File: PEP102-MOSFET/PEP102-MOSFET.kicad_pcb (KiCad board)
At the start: 2 copper layers, 45 x 45 mm, 22 parts, among them J1 Screw_Terminal_01x02, J2 Screw_Terminal_01x02, J3 Screw_Terminal_01x02, J4 Screw_Terminal_01x02, J5 Screw_Terminal_01x02, Q13 AO3400A, Q8 AO3401A

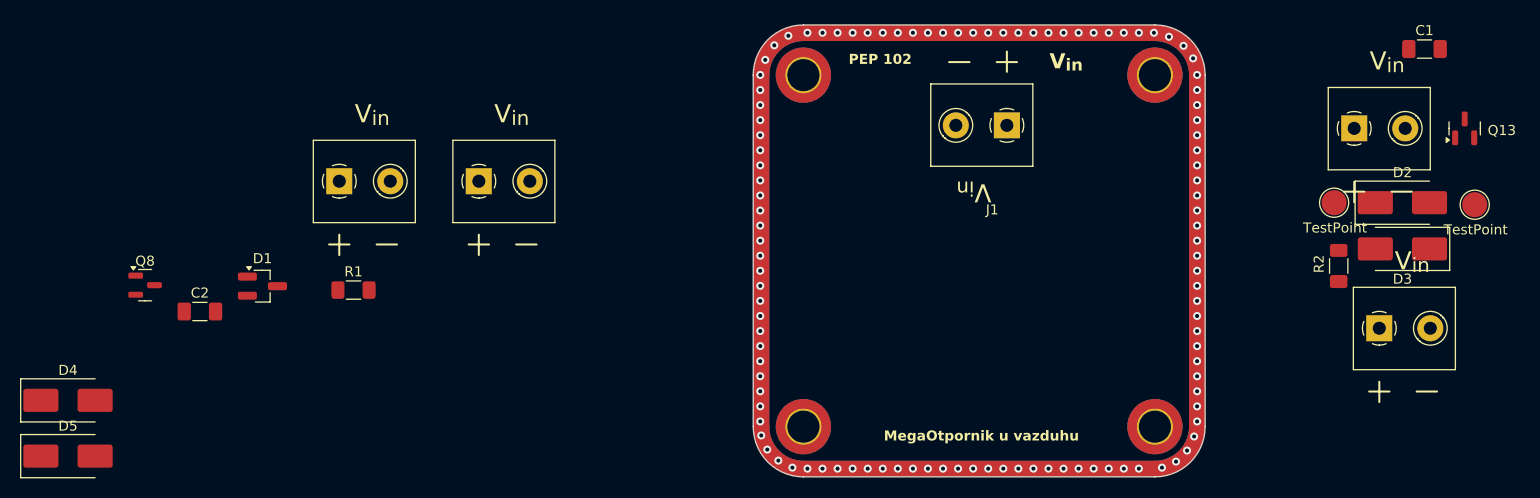
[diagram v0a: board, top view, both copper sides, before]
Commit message: Uklonjen PMOS sa PEP102 jer nema prostora.
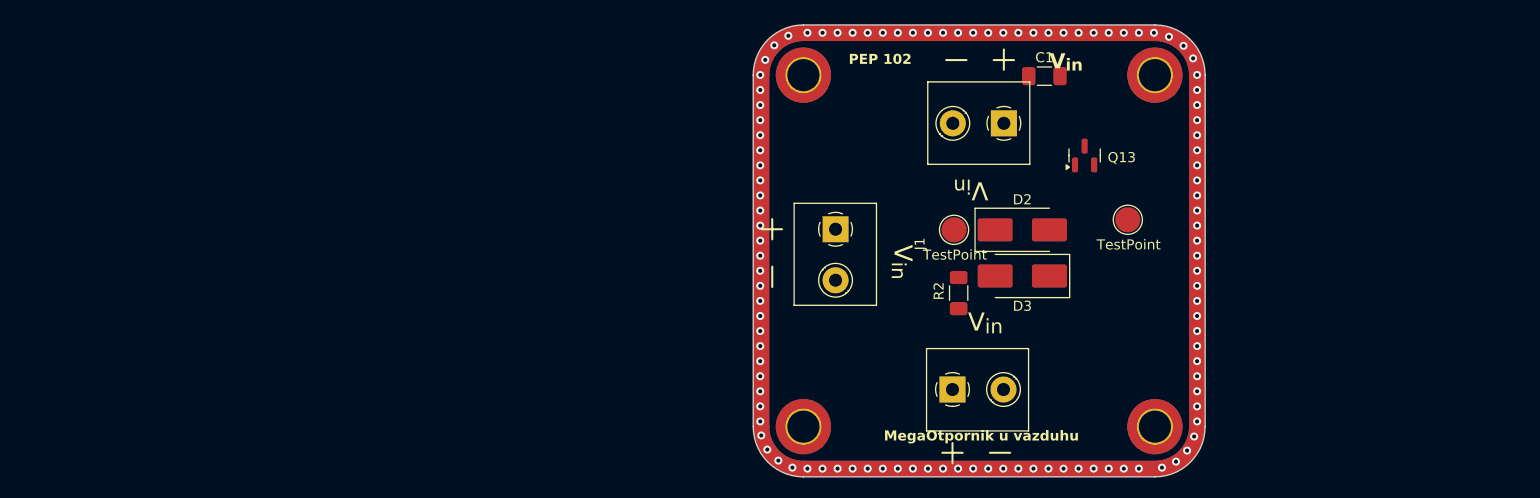
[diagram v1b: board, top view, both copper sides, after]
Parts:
- removed C2: 100n, Capacitor_SMD:C_1206_3216Metric_Pad1.33x1.80mm_HandSolder
- removed D1: PSM712-LF-T7, Package_TO_SOT_SMD:SOT-23_Handsoldering
- removed D4, D5: P6SMB6.8CA/TR13, Diode_SMD:D_SMB_Handsoldering
- removed J4, J5: Screw_Terminal_01x02, PEP_library:TerminalBlock_Phoenix_MKDS-1,5-2-5.08_1x02_P5.08mm_Horizontal
- removed Q8: AO3401A, Package_TO_SOT_SMD:SOT-23
- removed R1: 1k, Resistor_SMD:R_1206_3216Metric_Pad1.30x1.75mm_HandSolder
- moved J3 42.9 mm to (119.8, 136.3)
- moved R2 37.9 mm to (120.5, 126.7)
- moved D2 37.9 mm to (126.8, 120.4)
- moved D3 37.9 mm to (126.8, 125.0)
- moved C1 37.9 mm to (129.0, 105.1)
- moved Q13 37.9 mm to (133.0, 113.0)
- moved TP2 37.9 mm to (120.0, 120.4)
- moved J2 34.9 mm to (125.0, 109.8), turned to 180 degrees
- moved TP2 34.6 mm to (137.3, 119.4)
- moved J1 19.9 mm to (108.2, 120.3), turned to -90 degrees
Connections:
- J2 pad 1: VCC -> Net-(J2-Pin_1)
- J2 pad 2: Net-(J2-Pin_2) -> VCC
- Q13 pad 3: Net-(J2-Pin_2) -> Net-(J2-Pin_1)

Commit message: Placement done.
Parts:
- removed D2, D3: P6SMB6.8CA/TR13, Diode_SMD:D_SMB_Handsoldering
- removed Q13: AO3400A, Package_TO_SOT_SMD:SOT-23
- removed the TP2 at (120.0, 120.4)
- added D14: PSM712-LF-T7, Package_TO_SOT_SMD:SOT-23, F.Cu at (123.8, 128.7)
- added Q19: 2N7002, Package_TO_SOT_SMD:SOT-23, F.Cu at (122.5, 122.5)
- added TP1: TestPoint, TestPoint:TestPoint_Pad_D4.0mm, F.Cu at (117.9, 123.4)
- added TP3: TestPoint, TestPoint:TestPoint_Pad_D4.0mm, F.Cu at (122.5, 118.0)
- TP2: footprint TestPoint:TestPoint_Pad_D2.5mm -> TestPoint:TestPoint_Pad_D4.0mm
- moved C1 24.3 mm to (112.1, 122.5), turned to -90 degrees
- moved TP2 11.1 mm to (126.9, 123.4)
- moved J2 5.39 mm to (122.5, 105.0), turned to 0 degrees
- moved R2 5.17 mm to (118.0, 131.2)
- moved J3 4.55 mm to (122.5, 140.0)
- moved J1 3.86 mm to (105.0, 122.5)
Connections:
- J2 pad 1: Net-(J2-Pin_1) -> VCC
- J2 pad 2: VCC -> Net-(J2-Pin_2)
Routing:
- net VCC: track 0.00 -> 28.4 mm
- net Net-(J2-Pin_2): track 0.00 -> 17.6 mm, vias 0 -> 1
- net Net-(Q19-G): track 0.00 -> 15.3 mm, vias 0 -> 1
- net NMOS_GATE: track 0.00 -> 8.09 mm
- net 0: track 0.00 -> 5.76 mm, vias 0 -> 112
- net (no net): vias 109 -> 0
- added copper zone on B.Cu, net 0
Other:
- board text added: "MOSFET"
- board text removed: "MegaOtpornik u vazduhu"
- board text removed: "V_{in}"

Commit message: Done, kinda
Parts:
- added ?: , clipboard:cd909e86-6193-4077-a0b5-245ea85f982c, F.Cu at (115.8, 130.8)
- J2: footprint PEP_library:TerminalBlock_Phoenix_MKDS-1,5-2-5.08_1x02_P5.08mm_Horizontal -> PEP_library:Screw terminal
- moved J1 2.00 mm to (107.0, 122.5)
- moved J2 2.00 mm to (122.5, 107.0)
- moved J3 2.00 mm to (122.5, 138.0)
- moved C1 1.90 mm to (114.0, 122.5)
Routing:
- net VCC: track 28.4 -> 24.2 mm
- net NMOS_GATE: track 8.09 -> 5.89 mm
- net Net-(J2-Pin_2): track 17.6 -> 15.7 mm
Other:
- board text added: "V_{drain}"
- board text removed: "TestPoint"

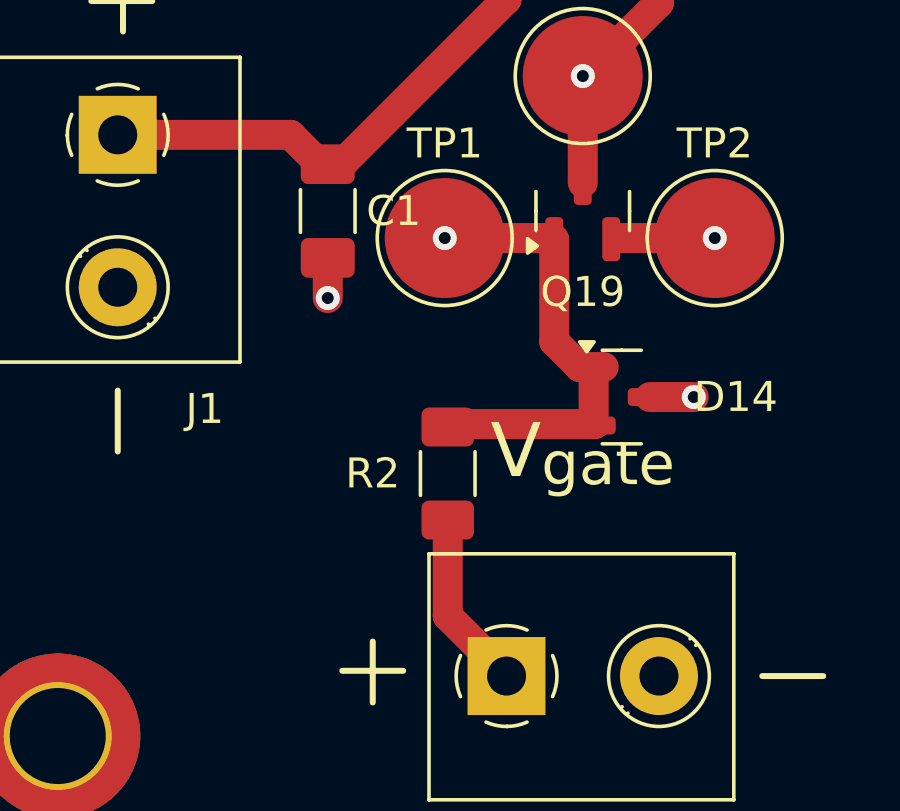
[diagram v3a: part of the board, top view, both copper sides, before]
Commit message: fixed mosfet error
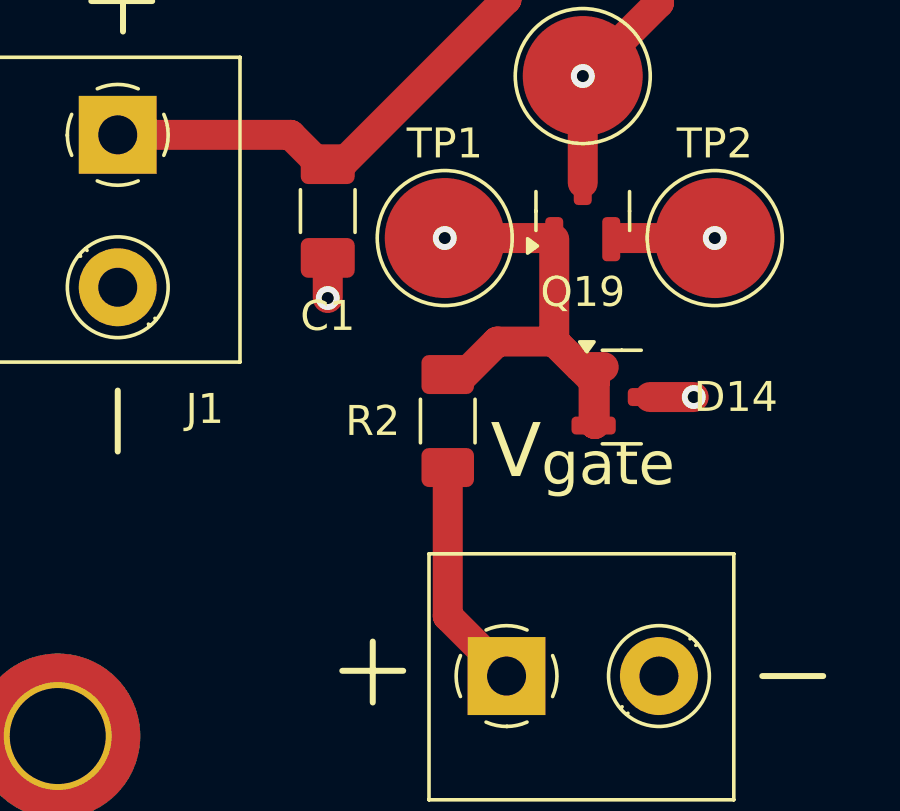
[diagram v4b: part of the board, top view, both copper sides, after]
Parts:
- moved R2 1.75 mm to (118.0, 129.5)
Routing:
- net Net-(Q19-G): track 15.3 -> 17.5 mm
- net NMOS_GATE: track 5.89 -> 7.19 mm
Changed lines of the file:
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@@
 	(footprint "Resistor_SMD:R_1206_3216Metric_Pad1.30x1.75mm_HandSolder"
 		(layer "F.Cu")
-		(at 118 131.25 90)
+		(at 118 129.5 90)
 		(descr "Resistor SMD 1206 (3216 Metric), square (rectangular) end terminal, IPC-7351 nominal with elongated pad for handsoldering. (Body size source: IPC-SM-782 page 72, https://www.pcb-3d.com/wordpress/wp-content/uploads/ipc-sm-782a_amendment_1_and_2.pdf), generated with kicad-footprint-generator")
 		(tags "resistor handsolder")
@@
 				(polygon
 					(pts
-						(xy 115.173094 130.66996) (xy 115.247417 130.684575) (xy 115.305495 130.706625) (xy 115.350401 130.735045)
-						(xy 115.387736 130.773292) (xy 115.414888 130.820072) (xy 115.432058 130.87718) (xy 115.438207 130.94717)
-						(xy 115.432378 131.011043) (xy 115.415787 131.065402) (xy 115.388992 131.112098) (xy 115.351481 131.152406)
-						(xy 115.301727 131.186902) (xy 115.237317 131.215409) (xy 115.508549 131.665) (xy 115.371223 131.665)
-						(xy 115.129423 131.248871) (xy 114.921084 131.248871) (xy 114.921084 131.665) (xy 114.804946 131.665)
-						(xy 114.804946 131.149159) (xy 114.921084 131.149159) (xy 115.080269 131.149159) (xy 115.161041 131.142675)
-						(xy 115.219302 131.12558) (xy 115.260581 131.100188) (xy 115.284839 131.073846) (xy 115.302618 131.041517)
-						(xy 115.31392 131.001931) (xy 115.317978 130.953337) (xy 115.31375 130.903913) (xy 115.302128 130.864927)
-						(xy 115.284054 130.834205) (xy 115.259543 130.810211) (xy 115.218013 130.787799) (xy 115.157611 130.772325)
-						(xy 115.072026 130.766369) (xy 114.921084 130.766369) (xy 114.921084 131.149159) (xy 114.804946 131.149159)
-						(xy 114.804946 130.664581) (xy 115.078864 130.664581)
+						(xy 115.173094 128.91996) (xy 115.247417 128.934575) (xy 115.305495 128.956625) (xy 115.350401 128.985045)
+						(xy 115.387736 129.023292) (xy 115.414888 129.070072) (xy 115.432058 129.12718) (xy 115.438207 129.19717)
+						(xy 115.432378 129.261043) (xy 115.415787 129.315402) (xy 115.388992 129.362098) (xy 115.351481 129.402406)
+						(xy 115.301727 129.436902) (xy 115.237317 129.465409) (xy 115.508549 129.915) (xy 115.371223 129.915)
+						(xy 115.129423 129.498871) (xy 114.921084 129.498871) (xy 114.921084 129.915) (xy 114.804946 129.915)
+						(xy 114.804946 129.399159) (xy 114.921084 129.399159) (xy 115.080269 129.399159) (xy 115.161041 129.392675)
+						(xy 115.219302 129.37558) (xy 115.260581 129.350188) (xy 115.284839 129.323846) (xy 115.302618 129.291517)
+						(xy 115.31392 129.251931) (xy 115.317978 129.203337) (xy 115.31375 129.153913) (xy 115.302128 129.114927)
+						(xy 115.284054 129.084205) (xy 115.259543 129.060211) (xy 115.218013 129.037799) (xy 115.157611 129.022325)
+						(xy 115.072026 129.016369) (xy 114.921084 129.016369) (xy 114.921084 129.399159) (xy 114.804946 129.399159)
+						(xy 114.804946 128.914581) (xy 115.078864 128.914581)
 					)
 				)
 				(polygon
 					(pts
-						(xy 116.257031 131.665) (xy 115.600567 131.665) (xy 115.600567 131.567424) (xy 115.863556 131.303337)
-						(xy 115.972322 131.189286) (xy 116.022008 131.129986) (xy 116.056237 131.077514) (xy 116.079405 131.028991)
-						(xy 116.093657 130.97843) (xy 116.098517 130.923234) (xy 116.092732 130.872043) (xy 116.076435 130.830581)
-						(xy 116.049974 130.796655) (xy 116.014972 130.771443) (xy 115.970987 130.755591) (xy 115.915457 130.749883)
-						(xy 115.854585 130.755069) (xy 115.79761 130.770399) (xy 115.741907 130.797365) (xy 115.673596 130.844832)
-						(xy 115.613512 130.76759) (xy 115.685938 130.716272) (xy 115.759546 130.680826) (xy 115.835227 130.659868)
-						(xy 115.914114 130.652857) (xy 115.984458 130.65792) (xy 116.043447 130.672135) (xy 116.093024 130.694533)
-						(xy 116.134726 130.724848) (xy 116.16932 130.763408) (xy 116.194033 130.80767) (xy 116.209306 130.858761)
-						(xy 116.214655 130.918288) (xy 116.208937 130.980221) (xy 116.191492 131.042485) (xy 116.161349 131.105989)
-						(xy 116.121593 131.165357) (xy 116.057498 131.24228) (xy 115.961924 131.340706) (xy 115.743327 131.554357)
-						(xy 115.743327 131.559792) (xy 116.257031 131.559792)
+						(xy 116.257031 129.915) (xy 115.600567 129.915) (xy 115.600567 129.817424) (xy 115.863556 129.553337)
+						(xy 115.972322 129.439286) (xy 116.022008 129.379986) (xy 116.056237 129.327514) (xy 116.079405 129.278991)
+						(xy 116.093657 129.22843) (xy 116.098517 129.173234) (xy 116.092732 129.122043) (xy 116.076435 129.080581)
+						(xy 116.049974 129.046655) (xy 116.014972 129.021443) (xy 115.970987 129.005591) (xy 115.915457 128.999883)
+						(xy 115.854585 129.005069) (xy 115.79761 129.020399) (xy 115.741907 129.047365) (xy 115.673596 129.094832)
+						(xy 115.613512 129.01759) (xy 115.685938 128.966272) (xy 115.759546 128.930826) (xy 115.835227 128.909868)
+						(xy 115.914114 128.902857) (xy 115.984458 128.90792) (xy 116.043447 128.922135) (xy 116.093024 128.944533)
+						(xy 116.134726 128.974848) (xy 116.16932 129.013408) (xy 116.194033 129.05767) (xy 116.209306 129.108761)
+						(xy 116.214655 129.168288) (xy 116.208937 129.230221) (xy 116.191492 129.292485) (xy 116.161349 129.355989)
+						(xy 116.121593 129.415357) (xy 116.057498 129.49228) (xy 115.961924 129.590706) (xy 115.743327 129.804357)
+						(xy 115.743327 129.809792) (xy 116.257031 129.809792)
 					)
 				)
@@
 		(tags "capacitor handsolder")
 		(property "Reference" "C1"
-			(at 0 -2.2 180)
+			(at 3.5 0 180)
 			(layer "F.SilkS")
 			(effects
@@
 				(polygon
 					(pts
-						(xy 115.923273 122.006721) (xy 115.857747 122.011478) (xy 115.800119 122.025116) (xy 115.749125 122.047083)
-						(xy 115.70376 122.077369) (xy 115.663338 122.116509) (xy 115.623266 122.173581) (xy 115.593612 122.241259)
-						(xy 115.574785 122.321584) (xy 115.568083 122.41711) (xy 115.574689 122.51599) (xy 115.593074 122.597631)
-						(xy 115.6217 122.664989) (xy 115.659918 122.72046) (xy 115.69878 122.758174) (xy 115.743415 122.787628)
-						(xy 115.79465 122.809208) (xy 115.853667 122.82274) (xy 115.92193 122.8275) (xy 115.991095 122.823729)
-						(xy 116.070104 122.811649) (xy 116.160311 122.789947) (xy 116.160311 122.891674) (xy 116.089986 122.912371)
-						(xy 116.005421 122.925799) (xy 115.904161 122.930631) (xy 115.815353 122.92464) (xy 115.738576 122.907617)
-						(xy 115.671963 122.880519) (xy 115.613991 122.843642) (xy 115.563565 122.796603) (xy 115.522529 122.741895)
-						(xy 115.4896 122.678024) (xy 115.46495 122.603581) (xy 115.449263 122.516817) (xy 115.443702 122.415706)
-						(xy 115.45052 122.313994) (xy 115.47005 122.224354) (xy 115.501405 122.144963) (xy 115.533877 122.089597)
-						(xy 115.572288 122.041694) (xy 115.616862 122.000569) (xy 115.6681 121.965811) (xy 115.723499 121.938871)
-						(xy 115.784181 121.919227) (xy 115.85092 121.907064) (xy 115.924617 121.902857) (xy 116.028122 121.909659)
-						(xy 116.119044 121.929107) (xy 116.199268 121.960254) (xy 116.150114 122.060027) (xy 116.073111 122.029984)
-						(xy 115.997764 122.012472)
+						(xy 113.723273 125.506721) (xy 113.657747 125.511478) (xy 113.600119 125.525116) (xy 113.549125 125.547083)
+						(xy 113.50376 125.577369) (xy 113.463338 125.616509) (xy 113.423266 125.673581) (xy 113.393612 125.741259)
+						(xy 113.374785 125.821584) (xy 113.368083 125.91711) (xy 113.374689 126.01599) (xy 113.393074 126.097631)
+						(xy 113.4217 126.164989) (xy 113.459918 126.22046) (xy 113.49878 126.258174) (xy 113.543415 126.287628)
+						(xy 113.59465 126.309208) (xy 113.653667 126.32274) (xy 113.72193 126.3275) (xy 113.791095 126.323729)
+						(xy 113.870104 126.311649) (xy 113.960311 126.289947) (xy 113.960311 126.391674) (xy 113.889986 126.412371)
+						(xy 113.805421 126.425799) (xy 113.704161 126.430631) (xy 113.615353 126.42464) (xy 113.538576 126.407617)
+						(xy 113.471963 126.380519) (xy 113.413991 126.343642) (xy 113.363565 126.296603) (xy 113.322529 126.241895)
+						(xy 113.2896 126.178024) (xy 113.26495 126.103581) (xy 113.249263 126.016817) (xy 113.243702 125.915706)
+						(xy 113.25052 125.813994) (xy 113.27005 125.724354) (xy 113.301405 125.644963) (xy 113.333877 125.589597)
+						(xy 113.372288 125.541694) (xy 113.416862 125.500569) (xy 113.4681 125.465811) (xy 113.523499 125.438871)
+						(xy 113.584181 125.419227) (xy 113.65092 125.407064) (xy 113.724617 125.402857) (xy 113.828122 125.409659)
+						(xy 113.919044 125.429107) (xy 113.999268 125.460254) (xy 113.950114 125.560027) (xy 113.873111 125.529984)
+						(xy 113.797764 125.512472)
 					)
 				)
 				(polygon
 					(pts
-						(xy 116.729946 122.915) (xy 116.619304 122.915) (xy 116.619304 122.201566) (xy 116.624739 122.0331)
-						(xy 116.592682 122.06308) (xy 116.430077 122.195949) (xy 116.369932 122.118279) (xy 116.634325 121.914581)
-						(xy 116.729946 121.914581)
+						(xy 114.529946 126.415) (xy 114.419304 126.415) (xy 114.419304 125.701566) (xy 114.424739 125.5331)
+						(xy 114.392682 125.56308) (xy 114.230077 125.695949) (xy 114.169932 125.618279) (xy 114.434325 125.414581)
+						(xy 114.529946 125.414581)
 					)
 				)
@@
 	)
 	(segment
-		(start 122.8625 127.75)
-		(end 122.8625 129.5625)
+		(start 119.65 126.85)
+		(end 118.5 128)
 		(width 1)
 		(layer "F.Cu")
@@
 	)
 	(segment
-		(start 122.9 129.6)
-		(end 118.3 129.6)
+		(start 122.8625 127.75)
+		(end 122.8625 129.5625)
 		(width 1)
 		(layer "F.Cu")
@@
 	)
 	(segment
+		(start 122.8625 129.5625)
+		(end 122.9 129.6)
+		(width 1)
+		(layer "F.Cu")
+		(net 3)
+	)
+	(segment
 		(start 122.4 127.7)
 		(end 123.2 127.7)
@@
 	)
 	(segment
-		(start 122.8625 129.5625)
-		(end 122.9 129.6)
+		(start 121.55 126.85)
+		(end 119.65 126.85)
+		(width 1)
+		(layer "F.Cu")
+		(net 3)
+	)
+	(segment
+		(start 122.9 129.6)
+		(end 122.9 128.2)
+		(width 1)
+		(layer "F.Cu")
+		(net 3)
+	)
+	(segment
+		(start 122.9 128.2)
+		(end 121.55 126.85)
 		(width 1)
 		(layer "F.Cu")
@@
 	)
 	(segment
-		(start 118 132.8)
+		(start 118 131.5)
 		(end 118 136)
 		(width 1)
